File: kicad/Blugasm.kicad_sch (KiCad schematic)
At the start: 46 parts, among them J1 PWR, J2 OLED, J3 I2C, J4 SERVO1, J5 PJ-102AH, J6 SERVO2, J7 BATT, Q1 DMG3415U, Q2 Q_NMOS_DGS, SW1 PWR, SW2 PEC11R-4225F-50024, U1 MCP73831-2-OT, U2 MP3V5050GP, U3 MCP6001-OT, U4 AP2112K-3.3

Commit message: cleanup
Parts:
- removed C10, C8, C9: 10nF, Capacitor_SMD:C_0603_1608Metric, symbol Device:C_Small
- removed D2: D_Schottky, Diode_SMD:D_SOD-123, symbol Device:D_Schottky
- removed J4: SERVO1, Connector_PinHeader_2.54mm:PinHeader_1x03_P2.54mm_Vertical, symbol Connector_Generic:Conn_01x03
- removed J6: SERVO2, Connector_PinHeader_2.54mm:PinHeader_1x03_P2.54mm_Vertical, symbol Connector_Generic:Conn_01x03
- removed SW1: PWR, Button_Switch_THT:SW_E-Switch_EG2219_DPDT_Angled, symbol Switch:SW_SPDT
- added BZ1: Buzzer, Buzzer_Beeper:Buzzer_12x9.5RM7.6, symbol Device:Buzzer
- added JP1, JP2: SolderJumper_3_Bridged12, Jumper:SolderJumper-3_P1.3mm_Bridged12_Pad1.0x1.5mm_NumberLabels, symbol Jumper:SolderJumper_3_Bridged12
- added R2: 1k, Resistor_SMD:R_0603_1608Metric, symbol Device:R
- added SW1: PWR, Button_Switch_THT:SW_E-Switch_EG2219_DPDT_Angled, symbol Switch:SW_DPDT_x2
- C1: renamed from C2; MPN (none) -> CL10B103KB8NNNC
- C2: renamed from C1; MPN (none) -> CL10A106MA8NRNC
- C3: MPN (none) -> CL10B105KA8NFNC
- C4: renamed from C5; MPN (none) -> CL10A106MA8NRNC
- C5: renamed from C4; MPN (none) -> CL10B334KO8NNNC
- C6: MPN (none) -> CL10A106MA8NRNC
- C7: MPN (none) -> CL10B104KB8NNWC
- D1: renamed from D3; MPN (none) -> MBR120ESFT1G
- D2: renamed from D1; value ORANGE -> GREEN; MPN (none) -> 150060VS75000
- D3: renamed from D4; value D_Schottky_Small -> SSB44-E3/52T; MPN (none) -> SSB44-E3/52T
- J1: symbol Connector:Barrel_Jack -> Connector:Barrel_Jack_Switch; MPN (none) -> PJ-102AH
- J2: renamed from J7; value BATT -> BAT
- J3: footprint Connector_PinHeader_2.54mm:PinHeader_1x04_P2.54mm_Vertical -> Connector_PinHeader_2.54mm:PinHeader_1x05_P2.54mm_Horizontal; symbol Connector_Generic:Conn_01x04 -> Connector_Generic:Conn_01x05
- J4: renamed from J5; value PJ-102AH -> MOTOR; symbol Connector:Barrel_Jack -> Connector:Barrel_Jack_Switch; MPN (none) -> PJ-102AH
- Q1: symbol Device:Q_PMOS_DGS -> Device:Q_PMOS_GSD; MPN (none) -> DMG3415UQ-7
- Q2: value Q_NMOS_DGS -> PHB32N06LT,118; footprint Package_TO_SOT_SMD:SOT-223-3_TabPin2 -> Package_TO_SOT_SMD:TO-263-3_TabPin2; symbol Device:Q_NMOS_DGS -> Device:Q_NMOS_GDS; MPN (none) -> PHB32N06LT,118
- R1: renamed from R6; value 100K -> 100k; MPN (none) -> RC0603FR-07100KL
- R10: value NC -> 10k; MPN (none) -> RC0603FR-0710KL
- R11: value 10K -> 10k; MPN (none) -> RC0603FR-0710KL
- R12: renamed from R9; value 330 -> 100; MPN (none) -> RC0603FR-07100RL
- R13: renamed from R12; value 10K -> 10k; MPN (none) -> RC0603FR-0710KL
- R3: renamed from R1; value 1K -> 1k; MPN (none) -> RC0603FR-071KL
- R4: renamed from R7; value 100K -> 100k; MPN (none) -> RC0603FR-07100KL
- R5: renamed from R3; MPN (none) -> RC0603FR-07750RL
- R6: renamed from R2; value 4.7K -> 4.7k; MPN (none) -> RC0603FR-074K7L
- R7: renamed from R4; value 100K -> 100k; MPN (none) -> RC0603FR-07100KL
- R8: renamed from R5; value 100K -> 100k; MPN (none) -> RC0603FR-07100KL
- R9: renamed from R8; value NC -> 10k; MPN (none) -> RC0603FR-0710KL
- RV1: value 10K -> GAIN; footprint Resistor_SMD:R_0603_1608Metric -> SaawLib:ST-4EB; MPN (none) -> ST-4ETB103
- U1: renamed from U2; footprint (none) -> SaawLib:MP3V5050; MPN (none) -> MP3V5050GP
- U2: renamed from U1; MPN (none) -> MCP73831T-2ACI/OT
- U3: renamed from U4; MPN (none) -> AP2112K-3.3TRG1
- U4: renamed from U3; MPN (none) -> MCP6001RT-I/OT
- renumbered J2 to J5
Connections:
- net Controller/SCL is gone; now on net SCL: J5.3 (SCL)
- net Controller/SDA is gone; now on net SDA: J5.4 (SDA)
- net VCC is gone; now on an unnamed net: D3.1 (K), J4.1
- net +BATT: now also J2.2 (Pin_2), Q1.3 (D); no longer J2.1 (Pin_1), Q1.1 (D)
- net AUX_MOT: now also R11.1
- net GND: now also J2.1 (Pin_1), BZ1.2 (+), JP1.3 (B), JP2.1 (A), SW1.2 (B); no longer J2.2 (Pin_2), J5.1 (GND)
- net at D3.2 (A), J4.2: now also Q2.2 (D); no longer Q2.1 (D)
- net at R4.1: now also C4.1, D1.1 (K), Q1.2 (S), U3.1 (VIN); no longer U3.3 (EN)
- net +3V3 renamed +3.3V
- net +3.3V: now also JP1.1 (A), JP2.3 (B); no longer J5.2 (VCC)
- net PWR_EN renamed ~{PWR_DIS}
- net ~{PWR_DIS}: now also U3.3 (EN), SW1.3 (C)
- net VBUS renamed +5V
- net +5V: now also Q1.1 (G), R2.2; no longer Q1.2 (G), R3.2
- net VB_SEN renamed VBAT_SENSE
- removed net VIN: C4.1, D1.1 (K), Q1.3 (S), U3.1 (VIN)
- new net: J5.1 (GND), JP2.2 (C)
- new net: Q2.1 (G), R12.2
- new net: R2.1, R3.2
- new net: J5.2 (VCC), JP1.2 (C)
- new net BUZZER: BZ1.1 (-)
- new net ~{INT}: J3.5 (Pin_5)
- no-connect marks 8 -> 6
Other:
- sheet Controller ports: added GPIO22, GPIO25, GPIO26, GPIO36; removed GPIO16, GPIO17, GPIO18, GPIO19, GPIO25/DAC1, GPIO26/DAC2, GPIO32, GPIO34, GPIO35, GPIO36/S_VP, GPIO39/S_VN
- note added: "Enables/disables the 3.3V reg"
- note added: "LiPo Charger / Monitoring"
- note added: "OLED Power Pin Flipping - Set JP1/JP2 to 2-1 for -/+ (default) - Set JP1/JP2 to 2-3 for +/-"
- note removed: "Aux. Power / Power Switch"
- note removed: "Enables the 3.3V reg"
- note removed: "LiPo Charger"
- note removed: "Mounting Holes"
- note removed: "TODOs: - Add alt power reg for aux power jack (NCP1117-5.0 or 3.3 ?)"
- company: (none) -> saawsm
- moved on the sheet: C2, C4, C6, D1, D2, D3, H1, H2, H3, H4, J2, J5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

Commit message: add pcb
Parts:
- removed R3: 1k, Resistor_SMD:R_0603_1608Metric, symbol Device:R
- added C6: 10uF, Capacitor_SMD:C_0603_1608Metric, symbol Device:C_Small
- added NT1: 0.5mm, NetTie:NetTie-2_SMD_Pad0.5mm, symbol Device:NetTie_2
- added R23: 100, Resistor_SMD:R_0603_1608Metric, symbol Device:R
- BZ1: MOUSER (none) -> 497-IE122303-1
- C1: LCSC (none) -> C1589; MOUSER (none) -> 187-CL10B103KB8NNNC
- C2, C4: LCSC (none) -> C96446; MOUSER (none) -> 187-CL10A106MA8NRNC
- C3: LCSC (none) -> C307479; MOUSER (none) -> 187-CL10B105KA8NFNC
- C5: LCSC (none) -> C159798; MOUSER (none) -> 187-CL10B334KO8NNNC
- C7: renamed from C6; LCSC (none) -> C96446; MOUSER (none) -> 187-CL10A106MA8NRNC
- C8: renamed from C7; LCSC (none) -> C1591; MOUSER (none) -> 187-CL10B104KB8NNNC
- D1: value MBR120 -> SS24FL; symbol Device:D_Zener -> Device:D_Schottky; LCSC (none) -> C894433; MOUSER (none) -> 512-SS24FL; MPN MBR120ESFT1G -> SS24FL
- D2: MOUSER (none) -> 710-150060VS75000
- D3: value SSB44-E3/52T -> SSB44-E3; footprint Diode_SMD:D_SOD-123 -> Diode_SMD:D_SMB; LCSC (none) -> C466999; MOUSER (none) -> 625-SSB44-E3
- J1: MOUSER (none) -> 490-PJ-102AH
- J5: renamed from J4; MOUSER (none) -> 490-PJ-102AH
- JP1, JP2: now left out of the parts list
- Q1: LCSC (none) -> C459537; MOUSER (none) -> 621-DMG3415UQ-7
- Q2: LCSC (none) -> C552626; MOUSER (none) -> 771-PHB32N06LT118
- R1: LCSC (none) -> C14675; MOUSER (none) -> 603-RC0603FR-07100KL
- R10: renamed from R11; LCSC (none) -> C98220; MOUSER (none) -> 603-RC0603FR-0710KL
- R11: renamed from R12; LCSC (none) -> C105588; MOUSER (none) -> 603-RC0603FR-07100RL
- R12: renamed from R13; LCSC (none) -> C98220; MOUSER (none) -> 603-RC0603FR-0710KL
- R2: value 1k -> 4.7k; LCSC (none) -> C99782; MOUSER (none) -> 603-RC0603FR-074K7L; MPN RC0603FR-071KL -> RC0603FR-074K7L
- R3: renamed from R4; LCSC (none) -> C14675; MOUSER (none) -> 603-RC0603FR-07100KL
- R4: renamed from R5; LCSC (none) -> C114635; MOUSER (none) -> 603-RC0603FR-07750RL
- R5: renamed from R6; LCSC (none) -> C99782; MOUSER (none) -> 603-RC0603FR-074K7L
- R6: renamed from R7; LCSC (none) -> C14675; MOUSER (none) -> 603-RC0603FR-07100KL
- R7: renamed from R8; LCSC (none) -> C14675; MOUSER (none) -> 603-RC0603FR-07100KL
- R8: renamed from R9; LCSC (none) -> C98220; MOUSER (none) -> 603-RC0603FR-0710KL
- R9: renamed from R10; LCSC (none) -> C98220; MOUSER (none) -> 603-RC0603FR-0710KL
- RV1: LCSC (none) -> C2922095; MOUSER (none) -> 229-ST-4ETB103
- SW1: LCSC (none) -> C3664594; MOUSER (none) -> 612-EG2219
- SW2: value PEC11R-4225F-50024 -> PEC11R-4220K-S0024; MOUSER (none) -> 652-PEC11R-4220K-S24; MPN PEC11R-4215F-S0024 -> PEC11R-4220K-S0024
- U1: MOUSER (none) -> 841-MP3V5050GP
- U2: LCSC (none) -> C424093; MOUSER (none) -> 579-MCP73831T-2ACIOT
- U3: LCSC (none) -> C51118; MOUSER (none) -> 621-AP2112K-3.3TRG1
- U4: LCSC (none) -> C154973; MOUSER (none) -> 579-MCP6001RT-I/OT
- renumbered J5 to J4
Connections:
- net +5V: now also R2.1, C6.1; no longer R2.2
- net GND: now also C6.2, NT1.1; no longer J1.2, Q2.3 (S), R10.2
- net P_SENSE: now also R23.2; no longer RV1.3, U4.1
- net at D2.2 (A): now also R2.2
- net CHG: no longer names the net of D2.1 (K), U2.1 (STAT)
- new net: R23.1, RV1.3, U4.1
- new net GND1: J1.2, NT1.2, Q2.3 (S), R10.2
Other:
- sheet Controller ports: added GPIO34, GPIO35; removed GPIO23, GPIO36
- note added: "Should really use an external ADC (e.g. ADS1115) instead of the internal ESP32 ADC"
- note removed: "Enables/disables the 3.3V reg"
- moved on the sheet: C1, C3, C5, C8, D1, R4, RV1, SW1A, SW1B, U1, U4

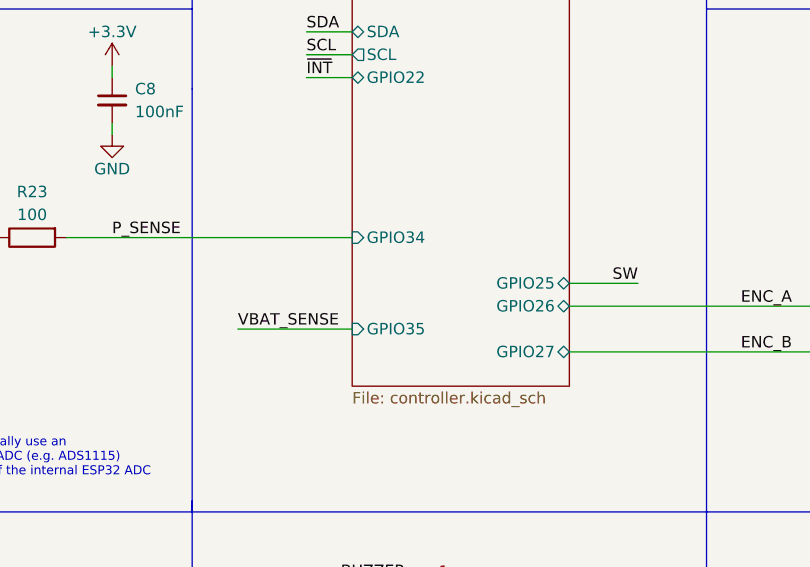
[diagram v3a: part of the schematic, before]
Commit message: use sensor_vp/vn for ADC
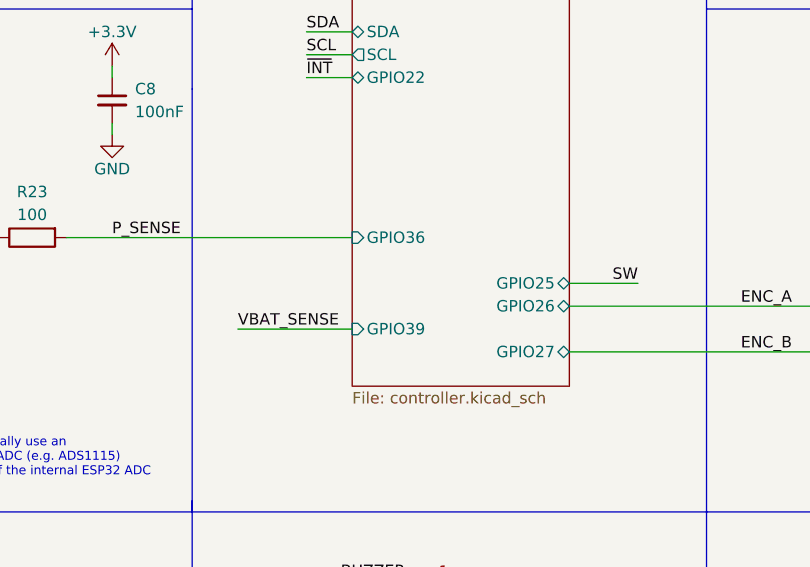
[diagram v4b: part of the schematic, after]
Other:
- sheet Controller ports: added GPIO36, GPIO39; removed GPIO34, GPIO35
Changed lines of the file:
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@@
       (effects (font (size 1.27 1.27)) (justify left))
     )
-    (pin "GPIO34" input (at 139.7 95.25 180)
+    (pin "GPIO36" input (at 139.7 95.25 180)
       (effects (font (size 1.27 1.27)) (justify left))
     )
@@
       (effects (font (size 1.27 1.27)) (justify right))
     )
-    (pin "GPIO35" input (at 139.7 105.41 180)
+    (pin "GPIO39" input (at 139.7 105.41 180)
       (effects (font (size 1.27 1.27)) (justify left))
     )
